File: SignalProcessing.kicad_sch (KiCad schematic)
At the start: 32 parts, among them J5 Header_100mil_1x06, J6 Header_100mil_1x06, U13 SD6210A, U14 ADS131M04IPWR, U15 AD9833BRMZ-REEL7, U16 AD826ARZ-REEL7, U17 LM27761DSGR

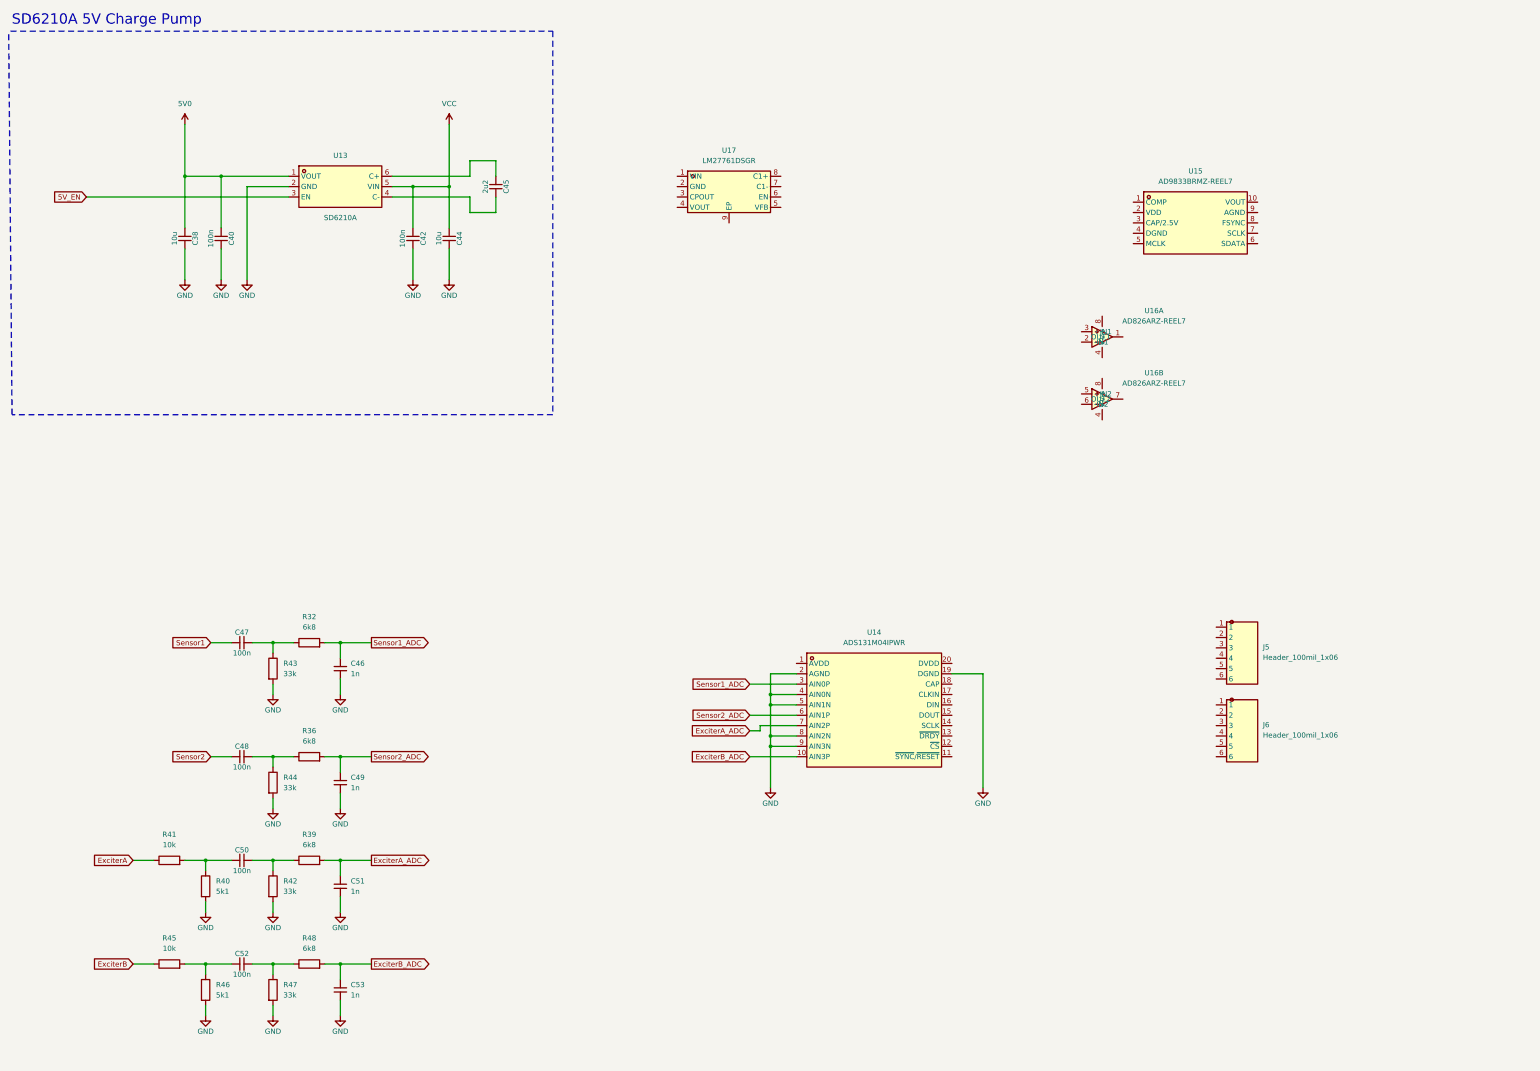
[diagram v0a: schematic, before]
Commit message: New components added, schematic being completed
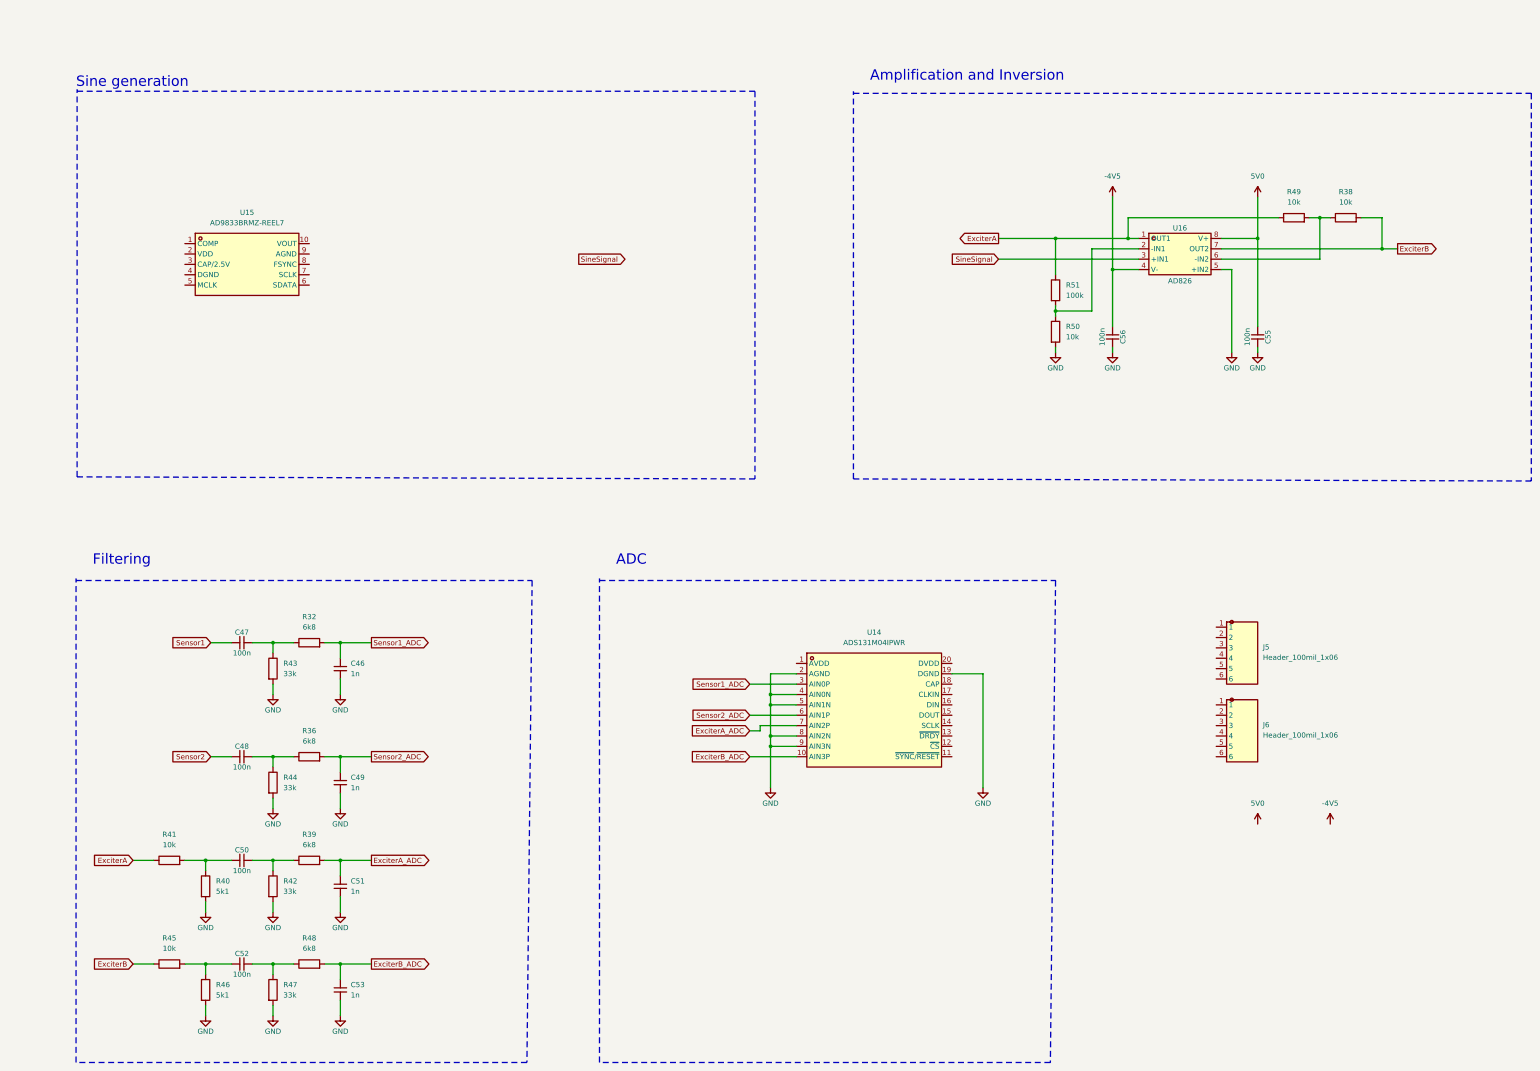
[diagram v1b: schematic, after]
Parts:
- removed C38, C44: 10u, sldrnrd:C_1206, symbol sldrnrd:Capacitor/C1206_10u
- removed C40, C42: 100n, sldrnrd:C_0603, symbol sldrnrd:Capacitor/C0603_100n
- removed C45: 2u2, sldrnrd:C_0805, symbol sldrnrd:Capacitor/C0805_2u2
- removed U13: SD6210A, sldrnrd:SOT-23-6, symbol sldrnrd:Power/ChargePump/SD6210A
- removed unit 2 of U16
- removed U17: LM27761DSGR, sldrnrd:WSON-8-2x2-EP, symbol sldrnrd:Power/ChargePump/LM27761DSGR
- added C55, C56: 100n, sldrnrd:C_0603, symbol sldrnrd:Capacitor/C0603_100n
- added R38, R49: 10k, sldrnrd:R_0603, symbol sldrnrd:Resistor/R0603_10k
- added R50: 10k, sldrnrd:R_0805, symbol sldrnrd:Resistor/R0805_10k
- added R51: 100k, sldrnrd:R_0805, symbol sldrnrd:Resistor/R0805_100k
- U16: value AD826ARZ-REEL7 -> AD826
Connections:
- net 5V0: now also U16.8 (V+), C55.1
- net ExciterA: now also U16.1 (OUT1), R49.1, R51.1
- net ExciterB: now also U16.7 (OUT2), R38.2
- net GND: now also U16.5 (+IN2), C55.2, C56.2, R50.2
- net at U16.2 (-IN1): now also R50.1, R51.2
- net SineSignal: now reaches U16.3 (+IN1)
- net -4V5: now reaches U16.4 (V-)
- net -4V5: now also C56.1
- new net: R38.1, R49.2, U16.6 (-IN2)
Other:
- note added: "ADC"
- note added: "Amplification and Inversion"
- note added: "Filtering"
- note added: "Sine generation"
- note removed: "SD6210A 5V Charge Pump"
- moved on the sheet: U15

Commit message: Schematic and component placement semi-final. Routing pending
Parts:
- added C57: 10u, sldrnrd:C_1206, symbol sldrnrd:Capacitor/C1206_10u
- added C58, C59, C63, C66, C67: 100n, sldrnrd:C_0603, symbol sldrnrd:Capacitor/C0603_100n
- added C60: 10n, sldrnrd:C_0603, symbol sldrnrd:Capacitor/C0603_10n
- added C61: 1n, sldrnrd:C_0603, symbol sldrnrd:Capacitor/C0603_1n
- added C62: 100p, sldrnrd:C_0603, symbol sldrnrd:Capacitor/C0603_100p
- added C64, C65: 1u, sldrnrd:C_0603, symbol sldrnrd:Capacitor/C0603_1u
- added C68: 220n, sldrnrd:C_0603, symbol sldrnrd:Capacitor/C0603_220n
- added R52: 6k8, sldrnrd:R_0603, symbol sldrnrd:Resistor/R0603_6k8
- added R53: 68k, sldrnrd:R_0603, symbol sldrnrd:Resistor/R0603_68k
- added R54: 10k, sldrnrd:R_0603, symbol sldrnrd:Resistor/R0603_10k
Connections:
- net -4V5: now also J5.2, J6.2
- net 5V0: now also J5.1, J6.1
- net ExciterA: now also J5.4, J6.4
- net ExciterB: now also J5.5, J6.5
- net ExciterB_ADC: now also U14.6 (AIN1P); no longer U14.10 (AIN3P)
- net GND: now also J5.3, J6.3, U15.4 (DGND), U15.9 (AGND), C57.2, C58.2, C59.2, C61.2, C62.2, C64.2, C65.2, C66.2, C67.2, C68.2, R54.2
- net Sensor1: now also J5.6
- net Sensor1_ADC: now also U14.10 (AIN3P); no longer U14.3 (AIN0P)
- net Sensor2: now also J6.6
- net Sensor2_ADC: now also U14.3 (AIN0P); no longer U14.6 (AIN1P)
- net SineSignal: now also C62.1, R53.2
- net at U15.1 (COMP): now also C60.2
- net at U15.10 (VOUT): now also C63.1
- net 3V3_Sensors: now reaches U15.2 (VDD)
- net 3V3_Sensors: now also U14.1 (AVDD), U14.20 (DVDD), C57.1, C58.1, C60.1, C64.1, C65.1, C66.1, C67.1
- net at U15.3 (CAP/2.5V): now also C59.1
- net DAC_Clock: now reaches U15.5 (MCLK)
- net DAC_MOSI: now reaches U15.6 (SDATA)
- net DAC_SCK: now reaches U15.7 (SCLK)
- net DAC_FSYNC: now reaches U15.8 (FSYNC)
- net ADC_SYNC_RESET: now reaches U14.11 (~{SYNC}/~{RESET})
- net ADC_CS: now reaches U14.12 (~{CS})
- net ADC_READY: now reaches U14.13 (~{DRDY})
- net ADC_SCK: now reaches U14.14 (SCLK)
- net ADC_MISO: now reaches U14.15 (DOUT)
- net ADC_MOSI: now reaches U14.16 (DIN)
- net ADC_CLOCK: now reaches U14.17 (CLKIN)
- net at U14.18 (CAP): now also C68.1
- new net: C63.2, R52.1, R54.1
- new net: C61.1, R52.2, R53.1
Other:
- note added: "Connectors"
- moved on the sheet: J5, U14, U15

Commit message: Board layout without errors
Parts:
- removed R40, R46: 5k1, sldrnrd:R_0603, symbol sldrnrd:Resistor/R0603_5k1
- added R38, R39, R40, R41: 10k, sldrnrd:R_0603, symbol sldrnrd:Resistor/R0603_10k
- renumbered C57 to C47, C58 to C48, C60 to C49, C59 to C50, C47 to C51, C48 to C52, C50 to C53, C52 to C54, C46 to C55, C49 to C56, C51 to C57, C53 to C58, C63 to C59, C61 to C60, C62 to C61, C66 to C62, C65 to C63, C67 to C65, C68 to C66, C56 to C67, C55 to C68, R41 to R36, R45 to R37, R43 to R42, R44 to R43, R42 to R44, R47 to R45, R32 to R46, R36 to R47, R39 to R48, R48 to R49, R54 to R50, R52 to R51, R53 to R52, R51 to R53, R50 to R54, R49 to R55, R38 to R56, U15 to U14, U14 to U15
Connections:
- net GND: now also R38.1, R39.1, R40.2, R41.2
- net at C54.1, R37.2: now also R39.2, R41.1
- net at C53.1, R36.2: now also R38.2, R40.1

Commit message: Fix stock/pinout issues, re-export fabrication files, apply JLC rotation corrections
- Replace out-of-stock parts (D2/D3 LED, U5, U10) with in-stock JLCPCB
  alternatives; add D5-D12 protection diodes
- Fix U2/DW01A footprint rotation on PCB
- Re-export gerbers, drill files, and JLCSMT BOM/CPL from current design
- BOM/CPL: DS1 uses header connector LCSC number only (display bought
  separately), U13 (LM35) and mounting holes excluded as do-not-place
- CPL rotations for U7, U5, Q3, U2 corrected per known JLCPCB
  per-part orientation quirks (see sldrnrd_kicad_lib/JLC_ROTATION_OFFSETS.md)
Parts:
- added D10, D11, D12, D5, D6, D7, D8, D9: 1N4148WS, sldrnrd:SOD-323, symbol sldrnrd:Diode/1N4148WS
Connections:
- net GND: now also D10.2 (A), D12.1 (K), D5.2 (A), D7.1 (K)
- net at C52.2, R43.1, R47.1: now also D11.2 (A), D9.1 (K)
- net at C51.2, R42.1, R46.1: now also D6.1 (K), D8.2 (A)
- new net: D5.1 (K), D6.2 (A)
- new net: D7.2 (A), D8.1 (K)
- new net: D11.1 (K), D12.2 (A)
- new net: D10.1 (K), D9.2 (A)
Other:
- moved on the sheet: C51, C52, C55, C56, R42, R43, R46, R47

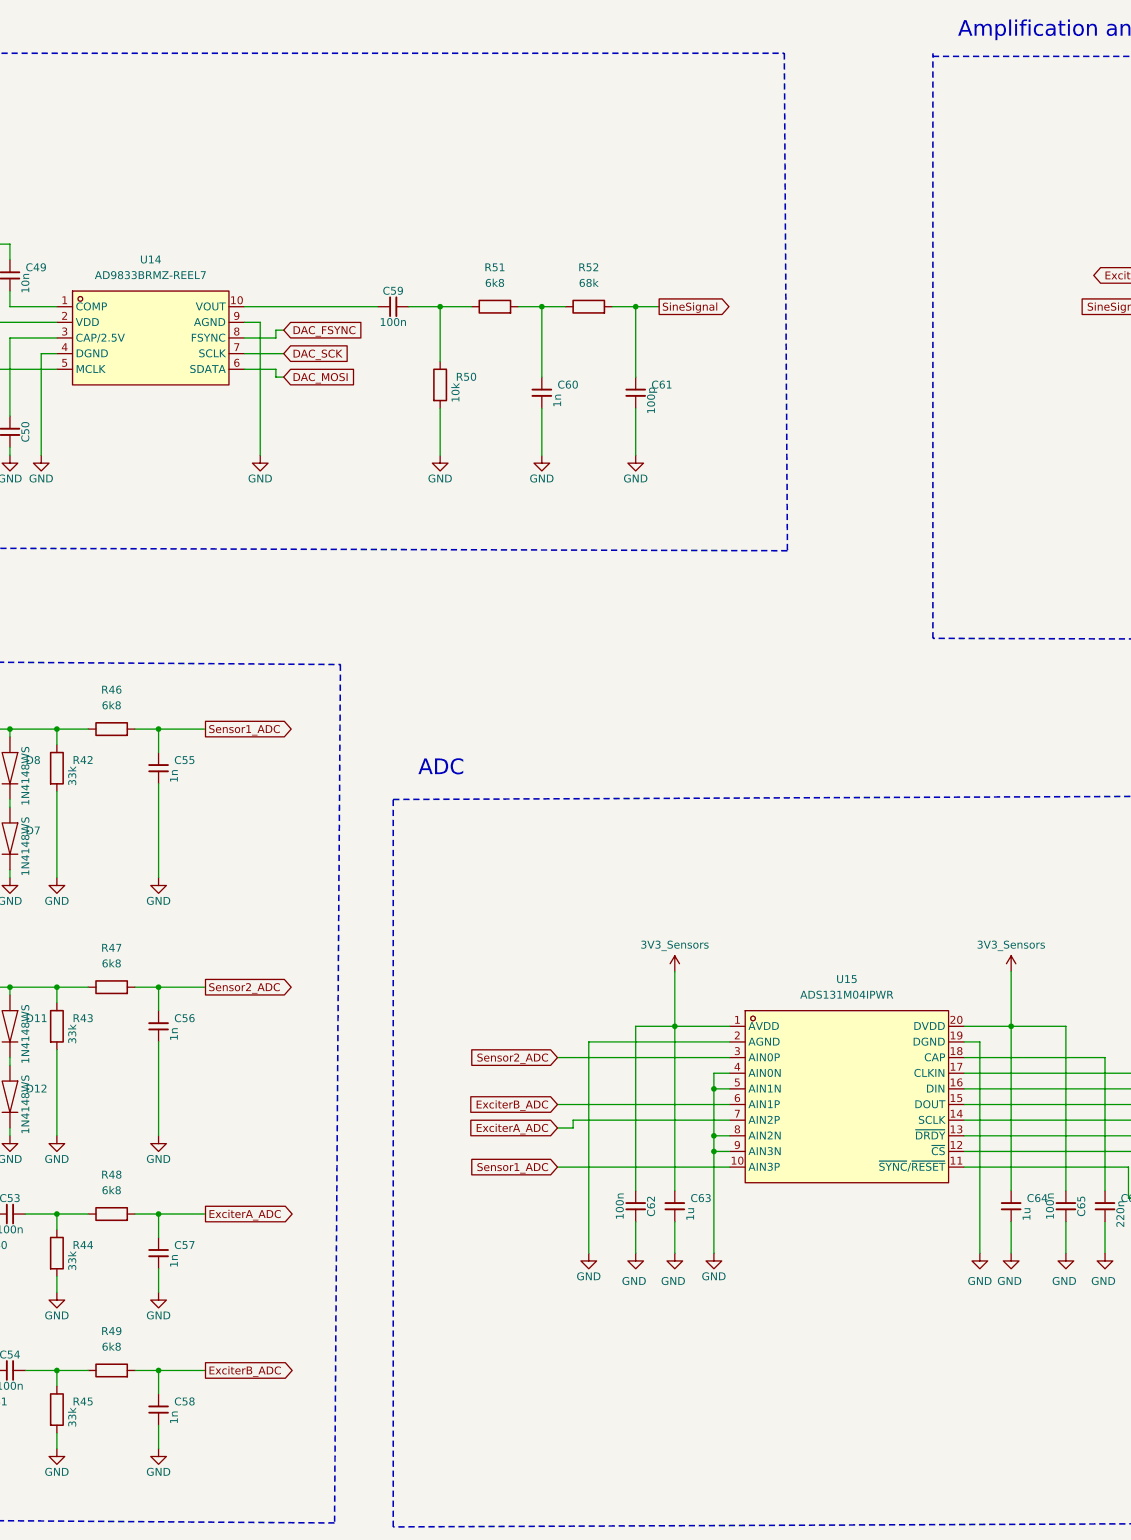
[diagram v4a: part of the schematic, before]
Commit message: Debug headers for SPI1, SPI2 and SPI3 added
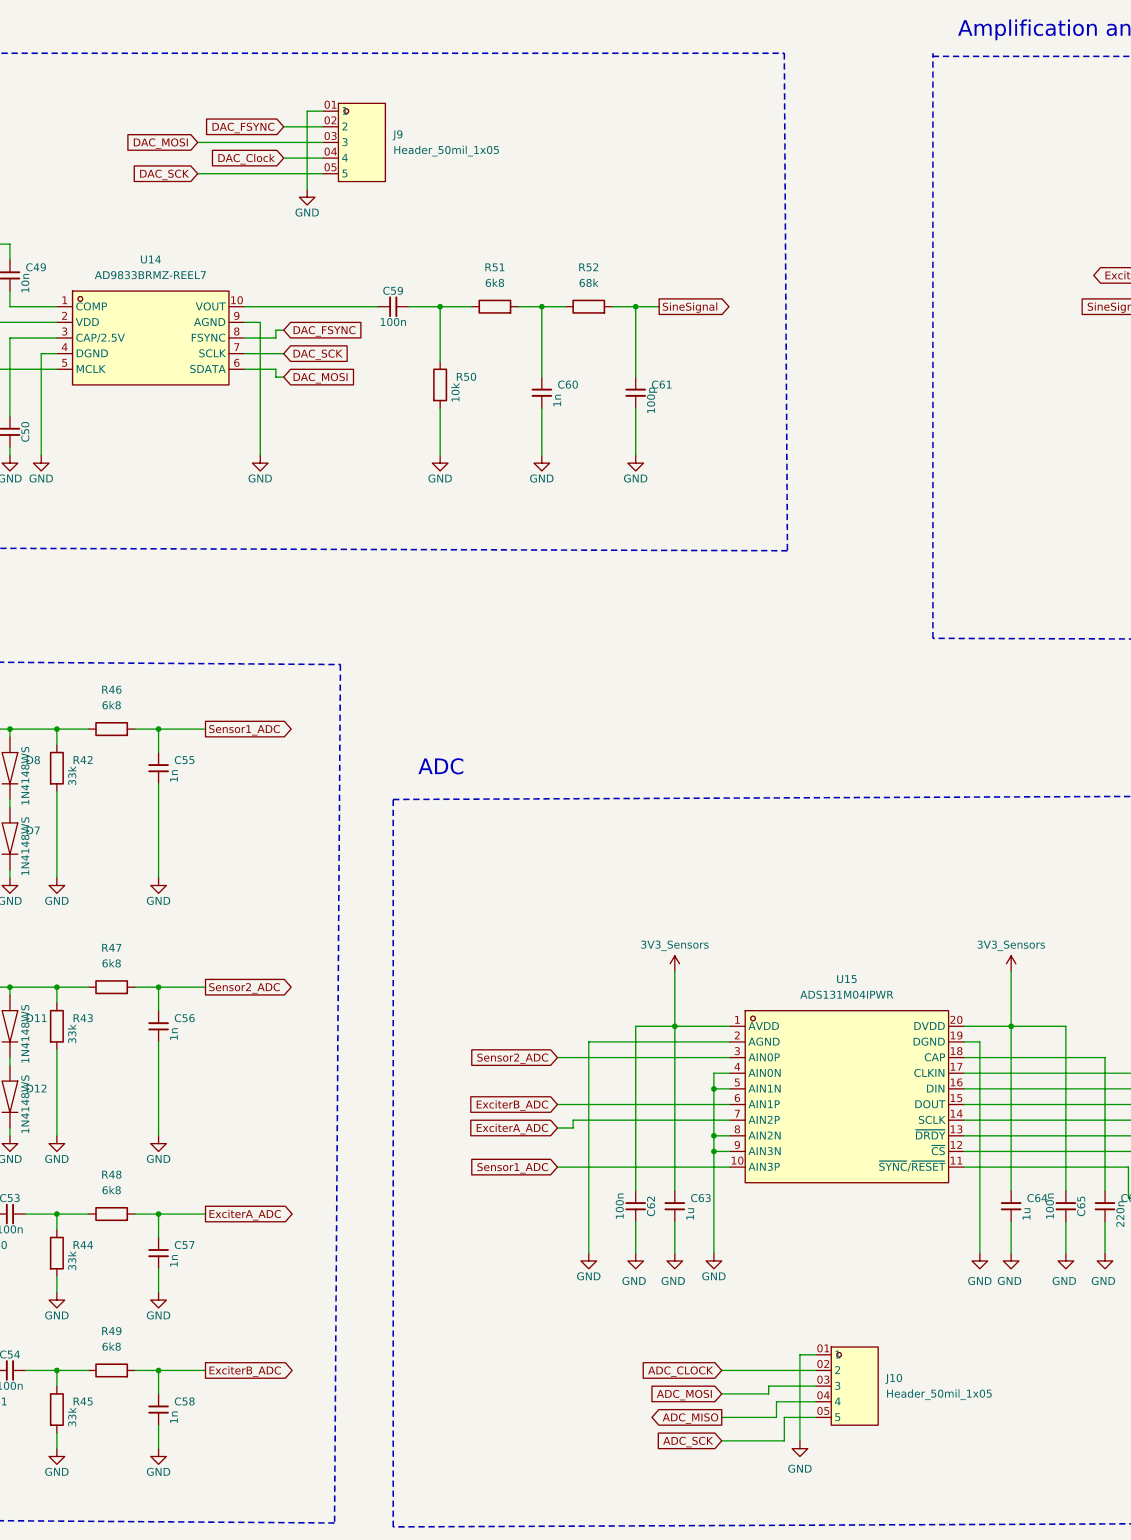
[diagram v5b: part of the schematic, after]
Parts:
- added J10, J9: Header_50mil_1x05, sldrnrd:Header_50mil_1x05, symbol sldrnrd:Connector/50Mil/Header_50mil_1x05
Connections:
- net ADC_CLOCK: now also J10.02 (2)
- net ADC_MISO: now also J10.04 (4)
- net ADC_MOSI: now also J10.03 (3)
- net ADC_SCK: now also J10.05 (5)
- net DAC_Clock: now also J9.04 (4)
- net DAC_FSYNC: now also J9.02 (2)
- net DAC_MOSI: now also J9.03 (3)
- net DAC_SCK: now also J9.05 (5)
- net GND: now also J10.01 (1), J9.01 (1)
